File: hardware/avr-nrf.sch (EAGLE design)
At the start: 73 parts, among them IC2 MAX1555, J1 J0026, U1 ATMEGA32U2AU, U2 NRF24L01SMD, U3 USB-MINIB-5PIN, U4 KSZ8851SNL, Y1 16M, Y2 8M, Y3 25M

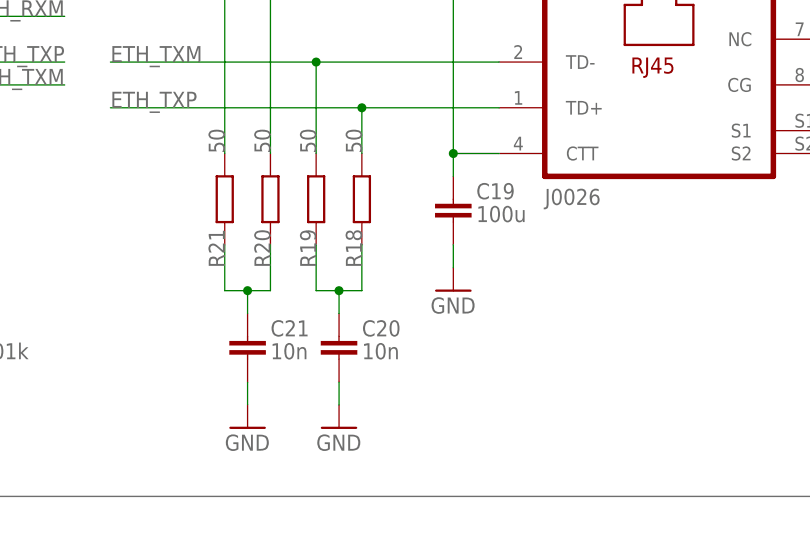
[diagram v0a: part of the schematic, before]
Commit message: hardware: fix eth cap values
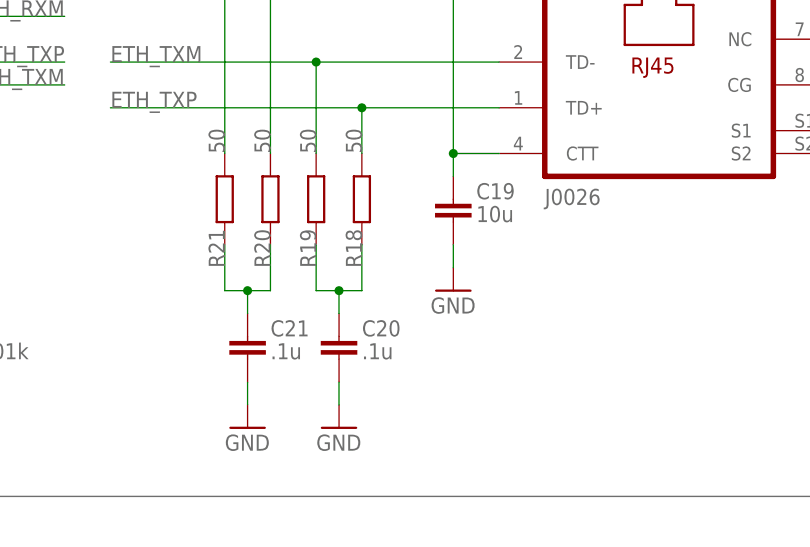
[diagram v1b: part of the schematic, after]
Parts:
- C19: value 100u -> 10u
- C20, C21: value 10n -> .1u
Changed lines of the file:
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@@
 <?xml version="1.0" encoding="utf-8"?>
 <!DOCTYPE eagle SYSTEM "eagle.dtd">
-<eagle version="6.0">
+<eagle version="6.1">
 <drawing>
 <settings>
@@
 <part name="R17" library="rcl" deviceset="R-EU_" device="R0603" value="330"/>
 <part name="P+9" library="supply1" deviceset="VCC" device=""/>
-<part name="C19" library="rcl" deviceset="C-EU" device="C0805" value="100u"/>
+<part name="C19" library="rcl" deviceset="C-EU" device="C0805" value="10u"/>
 <part name="GND33" library="supply1" deviceset="GND" device=""/>
 <part name="R18" library="rcl" deviceset="R-EU_" device="R0603" value="50"/>
-<part name="C20" library="rcl" deviceset="C-EU" device="C0805" value="10n"/>
-<part name="C21" library="rcl" deviceset="C-EU" device="C0805" value="10n"/>
+<part name="C20" library="rcl" deviceset="C-EU" device="C0805" value=".1u"/>
+<part name="C21" library="rcl" deviceset="C-EU" device="C0805" value=".1u"/>
 <part name="R19" library="rcl" deviceset="R-EU_" device="R0603" value="50"/>
 <part name="R20" library="rcl" deviceset="R-EU_" device="R0603" value="50"/>

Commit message: hw: update antenna symbol on schematics
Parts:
- U$1: value INVERTED_F_ANTENNA -> INVERTED_F_ANTENNA+5; device antenna:INVERTED_F_ANTENNA -> antenna:INVERTED_F_ANTENNA+5
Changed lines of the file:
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@@
 <grid distance="0.1" unitdist="inch" unit="inch" style="lines" multiple="1" display="no" altdistance="0.01" altunitdist="inch" altunit="inch"/>
 <layers>
-<layer number="1" name="Top" color="4" fill="1" visible="no" active="no"/>
-<layer number="16" name="Bottom" color="1" fill="1" visible="no" active="no"/>
-<layer number="17" name="Pads" color="2" fill="1" visible="no" active="no"/>
-<layer number="18" name="Vias" color="2" fill="1" visible="no" active="no"/>
-<layer number="19" name="Unrouted" color="6" fill="1" visible="no" active="no"/>
-<layer number="20" name="Dimension" color="15" fill="1" visible="no" active="no"/>
-<layer number="21" name="tPlace" color="7" fill="1" visible="no" active="no"/>
-<layer number="22" name="bPlace" color="7" fill="1" visible="no" active="no"/>
-<layer number="23" name="tOrigins" color="15" fill="1" visible="no" active="no"/>
-<layer number="24" name="bOrigins" color="15" fill="1" visible="no" active="no"/>
-<layer number="25" name="tNames" color="7" fill="1" visible="no" active="no"/>
-<layer number="26" name="bNames" color="7" fill="1" visible="no" active="no"/>
-<layer number="27" name="tValues" color="7" fill="1" visible="no" active="no"/>
-<layer number="28" name="bValues" color="7" fill="1" visible="no" active="no"/>
+<layer number="1" name="Top" color="4" fill="1" visible="yes" active="no"/>
+<layer number="16" name="Bottom" color="1" fill="1" visible="yes" active="no"/>
+<layer number="17" name="Pads" color="2" fill="1" visible="yes" active="no"/>
+<layer number="18" name="Vias" color="2" fill="1" visible="yes" active="no"/>
+<layer number="19" name="Unrouted" color="6" fill="1" visible="yes" active="no"/>
+<layer number="20" name="Dimension" color="15" fill="1" visible="yes" active="no"/>
+<layer number="21" name="tPlace" color="7" fill="1" visible="yes" active="no"/>
+<layer number="22" name="bPlace" color="7" fill="1" visible="yes" active="no"/>
+<layer number="23" name="tOrigins" color="15" fill="1" visible="yes" active="no"/>
+<layer number="24" name="bOrigins" color="15" fill="1" visible="yes" active="no"/>
+<layer number="25" name="tNames" color="7" fill="1" visible="yes" active="no"/>
+<layer number="26" name="bNames" color="7" fill="1" visible="yes" active="no"/>
+<layer number="27" name="tValues" color="7" fill="1" visible="yes" active="no"/>
+<layer number="28" name="bValues" color="7" fill="1" visible="yes" active="no"/>
 <layer number="29" name="tStop" color="7" fill="3" visible="no" active="no"/>
 <layer number="30" name="bStop" color="7" fill="6" visible="no" active="no"/>
@@
 <layer number="35" name="tGlue" color="7" fill="4" visible="no" active="no"/>
 <layer number="36" name="bGlue" color="7" fill="5" visible="no" active="no"/>
-<layer number="37" name="tTest" color="7" fill="1" visible="no" active="no"/>
-<layer number="38" name="bTest" color="7" fill="1" visible="no" active="no"/>
+<layer number="37" name="tTest" color="7" fill="1" visible="yes" active="no"/>
+<layer number="38" name="bTest" color="7" fill="1" visible="yes" active="no"/>
 <layer number="39" name="tKeepout" color="4" fill="11" visible="no" active="no"/>
 <layer number="40" name="bKeepout" color="1" fill="11" visible="no" active="no"/>
@@
 <layer number="44" name="Drills" color="7" fill="1" visible="no" active="no"/>
 <layer number="45" name="Holes" color="7" fill="1" visible="no" active="no"/>
-<layer number="46" name="Milling" color="3" fill="1" visible="no" active="no"/>
-<layer number="47" name="Measures" color="7" fill="1" visible="no" active="no"/>
-<layer number="48" name="Document" color="7" fill="1" visible="no" active="no"/>
-<layer number="49" name="Reference" color="7" fill="1" visible="no" active="no"/>
-<layer number="50" name="dxf" color="7" fill="1" visible="no" active="no"/>
-<layer number="51" name="tDocu" color="7" fill="1" visible="no" active="no"/>
-<layer number="52" name="bDocu" color="7" fill="1" visible="no" active="no"/>
-<layer number="53" name="tGND_GNDA" color="7" fill="9" visible="no" active="no"/>
-<layer number="54" name="bGND_GNDA" color="1" fill="9" visible="no" active="no"/>
-<layer number="56" name="wert" color="7" fill="1" visible="no" active="no"/>
+<layer number="46" name="Milling" color="3" fill="1" visible="yes" active="no"/>
+<layer number="47" name="Measures" color="7" fill="1" visible="yes" active="no"/>
+<layer number="48" name="Document" color="7" fill="1" visible="yes" active="no"/>
+<layer number="49" name="Reference" color="7" fill="1" visible="yes" active="no"/>
+<layer number="50" name="dxf" color="7" fill="1" visible="yes" active="no"/>
+<layer number="51" name="tDocu" color="7" fill="1" visible="yes" active="no"/>
+<layer number="52" name="bDocu" color="7" fill="1" visible="yes" active="no"/>
+<layer number="53" name="tGND_GNDA" color="7" fill="9" visible="yes" active="no"/>
+<layer number="54" name="bGND_GNDA" color="1" fill="9" visible="yes" active="no"/>
+<layer number="56" name="wert" color="7" fill="1" visible="yes" active="no"/>
 <layer number="91" name="Nets" color="2" fill="1" visible="yes" active="yes"/>
 <layer number="92" name="Busses" color="1" fill="1" visible="yes" active="yes"/>
@@
 <part name="TP3" library="testpad" deviceset="TP" device="TP08SQ"/>
 <part name="TP4" library="testpad" deviceset="TP" device="TP08SQ"/>
-<part name="U$1" library="antenna" deviceset="INVERTED_F_ANTENNA" device=""/>
+<part name="U$1" library="antenna" deviceset="INVERTED_F_ANTENNA" device="+5"/>
 <part name="GND29" library="supply1" deviceset="GND" device=""/>
 <part name="U4" library="balto" deviceset="KSZ8851SNL" device=""/>
